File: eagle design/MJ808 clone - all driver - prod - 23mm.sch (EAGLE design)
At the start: 32 parts, among them IC1 ATTINY4313-MMH, IC2 PRQV8.00CR1510Y00L, IC3 MCP2515, IC5 MCP2561-2, IC6 MAX16820, IC7 LDK320ADU50R, Q2 SiA456DJ, SW1 TL3305-844809

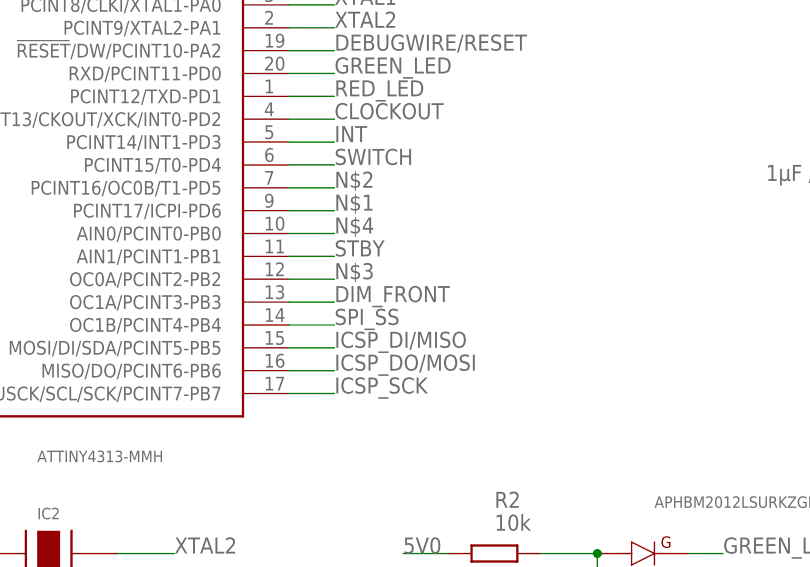
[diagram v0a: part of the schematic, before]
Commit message: - corrected dim_gate pin position: moved from pb3 to pb2; now it matches the POC board
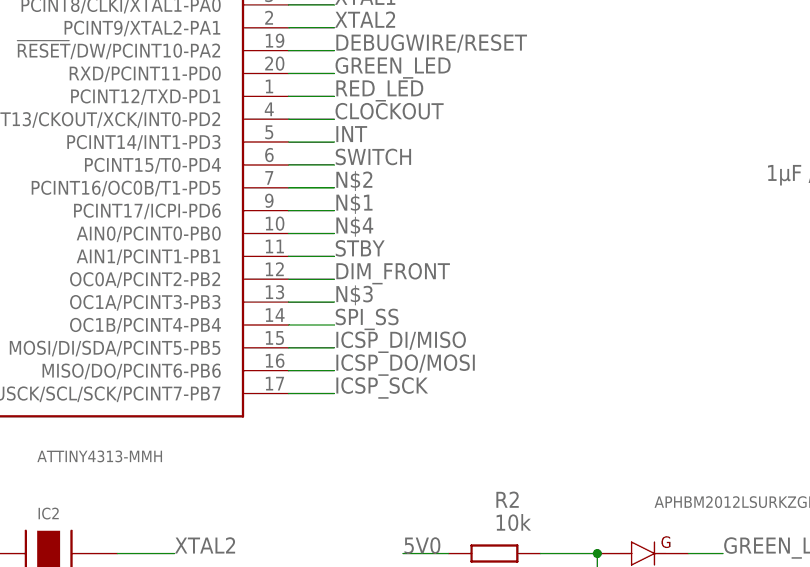
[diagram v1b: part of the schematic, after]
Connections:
- net DIM_FRONT: now also IC1.OC0A/PCINT2-PB2; no longer IC1.OC1A/PCINT3-PB3
- net N$3: now also IC1.OC1A/PCINT3-PB3; no longer IC1.OC0A/PCINT2-PB2
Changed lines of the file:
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@@
 </segment>
 <segment>
-<pinref part="IC1" gate="G$1" pin="OC1A/PCINT3-PB3"/>
-<wire x1="170.18" y1="162.56" x2="175.26" y2="162.56" width="0.1524" layer="91"/>
-<label x="175.26" y="162.56" size="1.778" layer="95"/>
+<pinref part="IC1" gate="G$1" pin="OC0A/PCINT2-PB2"/>
+<wire x1="170.18" y1="165.1" x2="175.26" y2="165.1" width="0.1524" layer="91"/>
+<label x="175.26" y="165.1" size="1.778" layer="95"/>
 </segment>
 </net>
@@
 </segment>
 </net>
-<net name="N$3" class="0">
-<segment>
-<pinref part="IC1" gate="G$1" pin="OC0A/PCINT2-PB2"/>
-<wire x1="170.18" y1="165.1" x2="175.26" y2="165.1" width="0.1524" layer="91"/>
-<label x="175.26" y="165.1" size="1.778" layer="95"/>
-</segment>
-</net>
 <net name="N$4" class="0">
 <segment>
@@
 </segment>
 </net>
+<net name="N$3" class="0">
+<segment>
+<pinref part="IC1" gate="G$1" pin="OC1A/PCINT3-PB3"/>
+<wire x1="170.18" y1="162.56" x2="175.26" y2="162.56" width="0.1524" layer="91"/>
+<label x="175.26" y="162.56" size="1.778" layer="95"/>
+</segment>
+</net>

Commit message: - resized battery and led vias, created gerber files
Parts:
- BAT+, GND: device signal testpoint:TP -> signal testpoint:TPTH-1.2MM
- CANH, CANL, LED+, LED-: device signal testpoint:TP -> signal testpoint:TPTH-0.9MM
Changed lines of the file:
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@@
 <grid distance="0.1" unitdist="inch" unit="inch" style="lines" multiple="1" display="no" altdistance="0.01" altunitdist="inch" altunit="inch"/>
 <layers>
-<layer number="1" name="Top" color="4" fill="1" visible="no" active="no"/>
-<layer number="2" name="Route2" color="1" fill="3" visible="no" active="no"/>
-<layer number="3" name="Route3" color="4" fill="3" visible="no" active="no"/>
-<layer number="4" name="Route4" color="1" fill="4" visible="no" active="no"/>
-<layer number="5" name="Route5" color="4" fill="4" visible="no" active="no"/>
-<layer number="6" name="Route6" color="1" fill="8" visible="no" active="no"/>
-<layer number="7" name="Route7" color="4" fill="8" visible="no" active="no"/>
-<layer number="8" name="Route8" color="1" fill="2" visible="no" active="no"/>
-<layer number="9" name="Route9" color="4" fill="2" visible="no" active="no"/>
-<layer number="10" name="Route10" color="1" fill="7" visible="no" active="no"/>
-<layer number="11" name="Route11" color="4" fill="7" visible="no" active="no"/>
-<layer number="12" name="Route12" color="1" fill="5" visible="no" active="no"/>
-<layer number="13" name="Route13" color="4" fill="5" visible="no" active="no"/>
-<layer number="14" name="Route14" color="1" fill="6" visible="no" active="no"/>
-<layer number="15" name="Route15" color="4" fill="6" visible="no" active="no"/>
-<layer number="16" name="Bottom" color="1" fill="1" visible="no" active="no"/>
-<layer number="17" name="Pads" color="2" fill="1" visible="no" active="no"/>
-<layer number="18" name="Vias" color="2" fill="1" visible="no" active="no"/>
-<layer number="19" name="Unrouted" color="6" fill="1" visible="no" active="no"/>
-<layer number="20" name="Dimension" color="24" fill="1" visible="no" active="no"/>
-<layer number="21" name="tPlace" color="7" fill="1" visible="no" active="no"/>
-<layer number="22" name="bPlace" color="7" fill="1" visible="no" active="no"/>
-<layer number="23" name="tOrigins" color="15" fill="1" visible="no" active="no"/>
-<layer number="24" name="bOrigins" color="15" fill="1" visible="no" active="no"/>
-<layer number="25" name="tNames" color="7" fill="1" visible="no" active="no"/>
-<layer number="26" name="bNames" color="7" fill="1" visible="no" active="no"/>
-<layer number="27" name="tValues" color="7" fill="1" visible="no" active="no"/>
-<layer number="28" name="bValues" color="7" fill="1" visible="no" active="no"/>
+<layer number="1" name="Top" color="4" fill="1" visible="yes" active="no"/>
+<layer number="2" name="Route2" color="1" fill="3" visible="yes" active="no"/>
+<layer number="3" name="Route3" color="4" fill="3" visible="yes" active="no"/>
+<layer number="4" name="Route4" color="1" fill="4" visible="yes" active="no"/>
+<layer number="5" name="Route5" color="4" fill="4" visible="yes" active="no"/>
+<layer number="6" name="Route6" color="1" fill="8" visible="yes" active="no"/>
+<layer number="7" name="Route7" color="4" fill="8" visible="yes" active="no"/>
+<layer number="8" name="Route8" color="1" fill="2" visible="yes" active="no"/>
+<layer number="9" name="Route9" color="4" fill="2" visible="yes" active="no"/>
+<layer number="10" name="Route10" color="1" fill="7" visible="yes" active="no"/>
+<layer number="11" name="Route11" color="4" fill="7" visible="yes" active="no"/>
+<layer number="12" name="Route12" color="1" fill="5" visible="yes" active="no"/>
+<layer number="13" name="Route13" color="4" fill="5" visible="yes" active="no"/>
+<layer number="14" name="Route14" color="1" fill="6" visible="yes" active="no"/>
+<layer number="15" name="Route15" color="4" fill="6" visible="yes" active="no"/>
+<layer number="16" name="Bottom" color="1" fill="1" visible="yes" active="no"/>
+<layer number="17" name="Pads" color="2" fill="1" visible="yes" active="no"/>
+<layer number="18" name="Vias" color="2" fill="1" visible="yes" active="no"/>
+<layer number="19" name="Unrouted" color="6" fill="1" visible="yes" active="no"/>
+<layer number="20" name="Dimension" color="24" fill="1" visible="yes" active="no"/>
+<layer number="21" name="tPlace" color="7" fill="1" visible="yes" active="no"/>
+<layer number="22" name="bPlace" color="7" fill="1" visible="yes" active="no"/>
+<layer number="23" name="tOrigins" color="15" fill="1" visible="yes" active="no"/>
+<layer number="24" name="bOrigins" color="15" fill="1" visible="yes" active="no"/>
+<layer number="25" name="tNames" color="7" fill="1" visible="yes" active="no"/>
+<layer number="26" name="bNames" color="7" fill="1" visible="yes" active="no"/>
+<layer number="27" name="tValues" color="7" fill="1" visible="yes" active="no"/>
+<layer number="28" name="bValues" color="7" fill="1" visible="yes" active="no"/>
 <layer number="29" name="tStop" color="7" fill="3" visible="no" active="no"/>
 <layer number="30" name="bStop" color="7" fill="6" visible="no" active="no"/>
@@
 <layer number="35" name="tGlue" color="7" fill="4" visible="no" active="no"/>
 <layer number="36" name="bGlue" color="7" fill="5" visible="no" active="no"/>
-<layer number="37" name="tTest" color="7" fill="1" visible="no" active="no"/>
-<layer number="38" name="bTest" color="7" fill="1" visible="no" active="no"/>
+<layer number="37" name="tTest" color="7" fill="1" visible="yes" active="no"/>
+<layer number="38" name="bTest" color="7" fill="1" visible="yes" active="no"/>
 <layer number="39" name="tKeepout" color="4" fill="11" visible="no" active="no"/>
 <layer number="40" name="bKeepout" color="1" fill="11" visible="no" active="no"/>
@@
 <layer number="44" name="Drills" color="7" fill="1" visible="no" active="no"/>
 <layer number="45" name="Holes" color="7" fill="1" visible="no" active="no"/>
-<layer number="46" name="Milling" color="3" fill="1" visible="no" active="no"/>
-<layer number="47" name="Measures" color="7" fill="1" visible="no" active="no"/>
-<layer number="48" name="Document" color="7" fill="1" visible="no" active="no"/>
-<layer number="49" name="Reference" color="7" fill="1" visible="no" active="no"/>
-<layer number="50" name="dxf" color="7" fill="1" visible="no" active="no"/>
-<layer number="51" name="tDocu" color="7" fill="1" visible="no" active="no"/>
-<layer number="52" name="bDocu" color="7" fill="1" visible="no" active="no"/>
-<layer number="53" name="tGND_GNDA" color="7" fill="9" visible="no" active="no"/>
-<layer number="54" name="bGND_GNDA" color="1" fill="9" visible="no" active="no"/>
-<layer number="56" name="wert" color="7" fill="1" visible="no" active="no"/>
-<layer number="57" name="tCAD" color="7" fill="1" visible="no" active="no"/>
-<layer number="59" name="tCarbon" color="7" fill="1" visible="no" active="no"/>
-<layer number="60" name="bCarbon" color="7" fill="1" visible="no" active="no"/>
+<layer number="46" name="Milling" color="3" fill="1" visible="yes" active="no"/>
+<layer number="47" name="Measures" color="7" fill="1" visible="yes" active="no"/>
+<layer number="48" name="Document" color="7" fill="1" visible="yes" active="no"/>
+<layer number="49" name="Reference" color="7" fill="1" visible="yes" active="no"/>
+<layer number="50" name="dxf" color="7" fill="1" visible="yes" active="no"/>
+<layer number="51" name="tDocu" color="7" fill="1" visible="yes" active="no"/>
+<layer number="52" name="bDocu" color="7" fill="1" visible="yes" active="no"/>
+<layer number="53" name="tGND_GNDA" color="7" fill="9" visible="yes" active="no"/>
+<layer number="54" name="bGND_GNDA" color="1" fill="9" visible="yes" active="no"/>
+<layer number="56" name="wert" color="7" fill="1" visible="yes" active="no"/>
+<layer number="57" name="tCAD" color="7" fill="1" visible="yes" active="no"/>
+<layer number="59" name="tCarbon" color="7" fill="1" visible="yes" active="no"/>
+<layer number="60" name="bCarbon" color="7" fill="1" visible="yes" active="no"/>
 <layer number="88" name="SimResults" color="9" fill="1" visible="yes" active="yes"/>
 <layer number="89" name="SimProbes" color="9" fill="1" visible="yes" active="yes"/>
@@
 <part name="ICSP" library="5034800600 FPC Connector" deviceset="5034800600" device="" value="5034800600 "/>
 <part name="R2" library="rcl" library_urn="urn:adsk.eagle:library:334" deviceset="R-EU_" device="R0402" package3d_urn="urn:adsk.eagle:package:23547/3" value="10k"/>
-<part name="GND" library="signal testpoint" deviceset="TP" device="" value="LiIon - Terminal"/>
-<part name="CANH" library="signal testpoint" deviceset="TP" device="" value="CAN high"/>
-<part name="CANL" library="signal testpoint" deviceset="TP" device="" value="CAN low"/>
-<part name="BAT+" library="signal testpoint" deviceset="TP" device="" value="LiIon + Terminal"/>
-<part name="LED+" library="signal testpoint" deviceset="TP" device="" value="LED anode"/>
-<part name="LED-" library="signal testpoint" deviceset="TP" device="" value="LED cathode"/>
+<part name="GND" library="signal testpoint" deviceset="TP" device="TH-1.2MM" value="LiIon - Terminal"/>
+<part name="CANH" library="signal testpoint" deviceset="TP" device="TH-0.9MM" value="CAN high"/>
+<part name="CANL" library="signal testpoint" deviceset="TP" device="TH-0.9MM" value="CAN low"/>
+<part name="BAT+" library="signal testpoint" deviceset="TP" device="TH-1.2MM" value="LiIon + Terminal"/>
+<part name="LED+" library="signal testpoint" deviceset="TP" device="TH-0.9MM" value="LED anode"/>
+<part name="LED-" library="signal testpoint" deviceset="TP" device="TH-0.9MM" value="LED cathode"/>
 <part name="LED1" library="APHBM2012LSURKZGKC" deviceset="APHBM2012LSURKZGKC" device="" value="APHBM2012LSURKZGKC"/>
 <part name="C2" library="rcl" library_urn="urn:adsk.eagle:library:334" deviceset="C-EU" device="C0402" package3d_urn="urn:adsk.eagle:package:23626/2" value="0.1μF"/>

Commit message: - finished MJ808 prod 4 layer rev.4a board
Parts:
- removed CANH: CAN high, signal testpoint:TPTH-0.9MM
- removed CANL: CAN low, signal testpoint:TPTH-0.9MM
- removed Q2: SiA456DJ, SIA456DJ-T1-GE3 N-Fet:SIA456DJ
- removed R10, R8: 10k, rcl:R-EU_R0402
- removed R13: 741X083331JP 330R, 74x-1133528 Resistor Array:741X083331JP
- added H: CAN high, signal testpoint:TPSMT-1.2MM
- added IC4: LDK320ADU50R, LDK320 5V LDO:LDK320SOT-23-5L
- added L: CAN low, signal testpoint:TPSMT-1.2MM
- BAT+, GND: device signal testpoint:TPTH-1.2MM -> signal testpoint:TPTH-0.9MM
- IC7: value LDK320ADU50R -> SiA456DJ; device LDK320 5V LDO:LDK320SOT-23-5L -> SIA456DJ-T1-GE3 N-Fet:SIA456DJ
- R1: value 10k -> 741X083331JP 330R; device rcl:R-EU_R0402 -> 74x-1133528 Resistor Array:741X083331JP
- R3: value 10k -> 741X083103JP 10k; device rcl:R-EU_R0402 -> 74x-1133528 Resistor Array:741X083331JP
- renumbered C7 to C3, C8 to C4, LED+ to AND, LED- to CTD, R11 to R5, R9 to R4
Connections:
- net 5V0: now also IC4.VOUT, R1.8, R3.6, R3.8; no longer IC7.VOUT, R10.1, R13.8, R3.1
- net BAT+: now also IC4.EN, IC4.VIN; no longer IC7.EN, IC7.VIN
- net CANH: now also H.TP$1; no longer CANH.TP$1
- net CANL: now also L.TP$1; no longer CANL.TP$1
- net DIM_FRONT: now also R3.2; no longer R8.1
- net DIM_FRONT_DRAIN: now also IC7.D; no longer Q2.D
- net DIM_FRONT_GATE: now also IC7.G; no longer Q2.G
- net GND: now also IC4.GND, IC7.S, R3.1, R3.3; no longer IC7.GND, Q2.S, R1.2, R8.2
- net ICSP_DI/MISO: now also R1.5; no longer R13.5
- net ICSP_DO/MOSI: now also R1.3; no longer R13.3
- net ICSP_SCK: now also R1.1; no longer R13.1
- net RESET: now also R3.5; no longer R3.2
- net SPI_MISO: now also R1.6; no longer R13.6
- net SPI_MOSI: now also R1.4; no longer R13.4
- net SPI_SCK: now also R1.2; no longer R13.2
- net SPI_SS: now also R1.7; no longer R13.7
- net STBY: now also R3.7; no longer R10.2
- net SWITCH: now also R3.4; no longer R1.1
